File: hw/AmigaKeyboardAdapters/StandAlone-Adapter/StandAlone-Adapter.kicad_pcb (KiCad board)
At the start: 2 copper layers, 78.7 x 58.4 mm, 55 parts, among them J1 RJ10, J2 Conn_02x03_Odd_Even, P1 CONN_01X02, Q1 BSS138, Q2 BSS138, Q3 BSS138, U1 AZ1117-3.3, U3 STM32F401RCTx

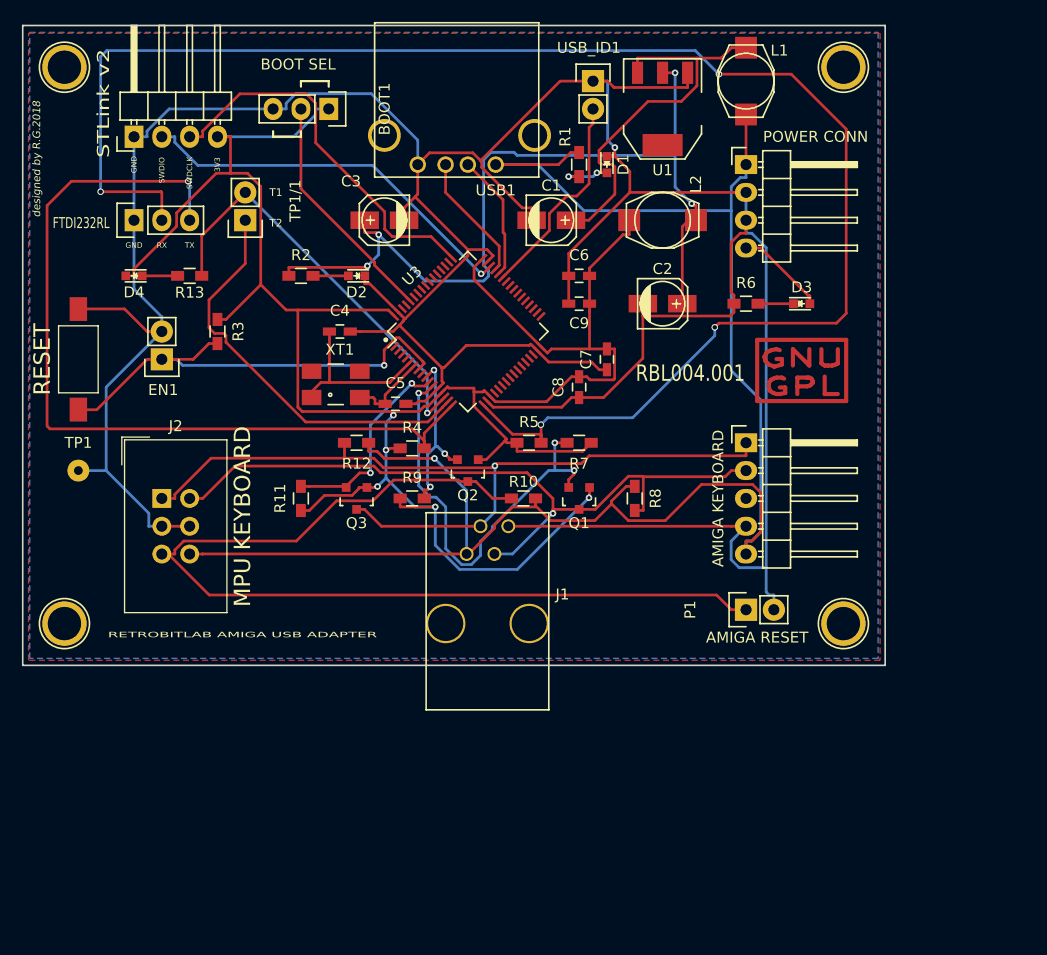
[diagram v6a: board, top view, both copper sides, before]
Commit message: REfactoring for new Crystal Oscillator & new 1208 footprints handsoldering
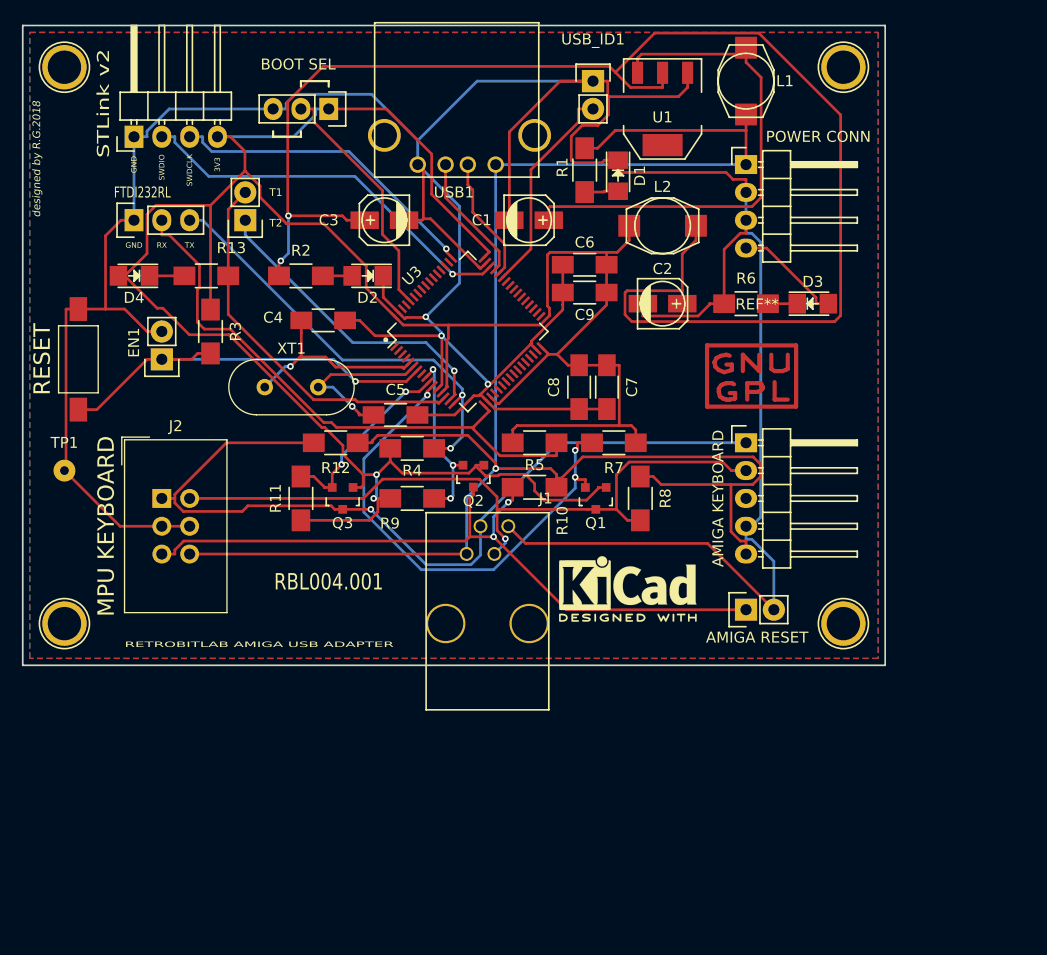
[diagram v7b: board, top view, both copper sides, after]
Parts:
- removed G***: LOGO, RetroBitLab:amigaLogo_BW_31x12mm-SilkScreenBack
- removed G***: LOGO, RetroBitLab:amigaWorkBench1-SIlkScreenBack
- removed GPLLOGO: Symbol_GNU-GPL_CopperTop_Small, Symbols:Symbol_GNU-GPL_CopperTop_Small
- added AMIGA: LOGO, RetroBitLab:amigaLogo_BW_31x12mm-SilkScreenBack, B.Cu at (150.5, 86.4)
- added REF**: Symbol_GNU-GPL_CopperTop_Small, Symbol:Symbol_GNU-GPL_CopperTop_Small, F.Cu at (175.8, 98.3)
- added WB: LOGO, RetroBitLab:amigaWorkBench1-SIlkScreenBack, B.Cu at (137.2, 111.1)
- added kicad: KiCad-Logo2_5mm_SilkScreen, Symbol:KiCad-Logo2_5mm_SilkScreen, F.Cu at (164.5, 117.5)
- C4, C5, C6, C7, C8, C9: footprint Capacitors_SMD:C_0603_HandSoldering -> Capacitors_SMD:C_1206_HandSoldering
- D1, D2, D3, D4: footprint LEDs:LED_0603 -> LEDs:LED_1206
- J2: footprint Connector_IDC:IDC-Header_2x03_P2.54mm_Vertical -> RetroBitLab:IDC-Header_2x03_P2.54mm_Vertical
- R1, R10, R11, R12, R13, R2, R3, R4, R5, R6, R7, R8, R9: footprint Resistors_SMD:R_0603_HandSoldering -> Resistors_SMD:R_1206_HandSoldering
- USB1: footprint Connect:USB_A -> RetroBitLab:USB_A_UP
- XT1: footprint Crystals:Crystal_SMD_0603_4Pads -> RetroBitLab:Crystal_HC49-4H_Vertical_3D
- moved XT1 6.48 mm to (131.3, 99.1)
- moved R7 3.17 mm to (163.2, 104.1)
- moved C7 2.54 mm to (162.6, 99.1)
- moved C1 2.03 mm to (155.4, 83.8)
- moved R12 1.91 mm to (137.8, 104.1)
- moved C4 1.83 mm to (136.7, 93.0)
- moved Q1 1.52 mm to (161.5, 109.2)
- moved R13 1.52 mm to (126.0, 88.9)
- moved D1 1.44 mm to (163.6, 79.8)
- moved R10 1.44 mm to (156.0, 108.2)
- moved TP1 1.27 mm to (113.0, 106.7)
- moved Q3 1.27 mm to (138.4, 109.2)
- moved C6 1.14 mm to (160.5, 87.9)
- moved C9 1.14 mm to (160.5, 90.4)
- moved D2 1.02 mm to (140.7, 88.9)
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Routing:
- net UART_RX_TTL: track 150.0 -> 53.2 mm, vias 4 -> 0
- net Net-(C2-Pad1): track 78.7 -> 139.7 mm, vias 4 -> 2
- net UART_TX_TTL: track 78.3 -> 39.9 mm, vias 1 -> 2
- net VCC3V3: track 203.1 -> 241.5 mm, vias 5 -> 2
- net KBD_RESET: track 90.5 -> 67.0 mm, vias 0 -> 2
- net GND: track 332.7 -> 344.5 mm, vias 1 -> 3
- net +5V: track 35.7 -> 46.5 mm
- net TP2: track 37.8 -> 28.6 mm, vias 0 -> 1
- net Net-(C5-Pad1): track 7.35 -> 15.7 mm, vias 0 -> 1
- net VCC5V: track 159.1 -> 165.9 mm
- net KBD_3v3_DATA: track 39.4 -> 46.1 mm
- net SWDCLK: track 35.2 -> 29.1 mm, vias 0 -> 1
- net Net-(EN1-Pad1): track 43.1 -> 38.8 mm
- net TP1: track 38.5 -> 35.2 mm, vias 1 -> 0
- net Net-(C4-Pad1): track 15.3 -> 18.4 mm, vias 0 -> 1
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
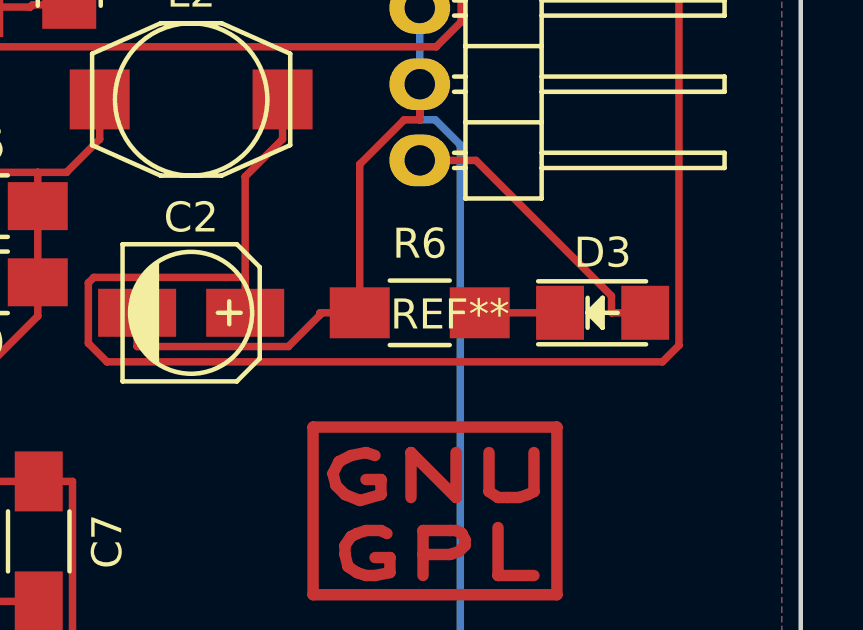
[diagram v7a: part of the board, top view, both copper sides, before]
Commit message: Hide the LOGO label REF** on SilkScreen
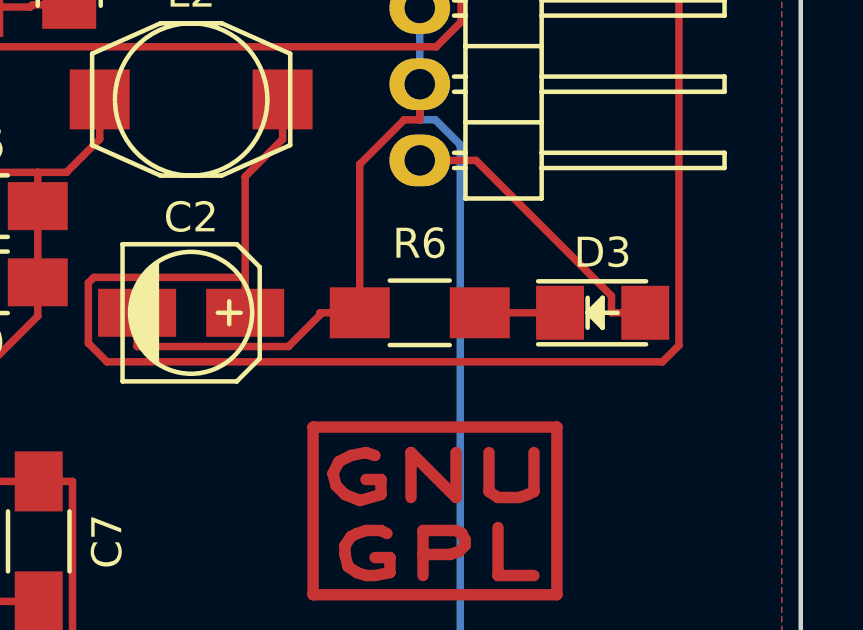
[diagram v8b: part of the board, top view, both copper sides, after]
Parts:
- renumbered REF** to GPL
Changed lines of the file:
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@@
     (tags "Symbol, GNU-GPL, Copper Top, Small,")
     (attr virtual)
-    (fp_text reference REF** (at 0.50038 -6.79958) (layer F.SilkS)
+    (fp_text reference GPL (at 0.50038 -6.79958) (layer F.SilkS) hide
       (effects (font (size 1 1) (thickness 0.15)))
     )
